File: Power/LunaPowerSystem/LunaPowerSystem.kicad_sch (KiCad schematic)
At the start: 16 parts, among them U1 Power Distribution Panel, U2 E-STOP, U3 Mini Power Distribution Panel, U4 Jetson Nano

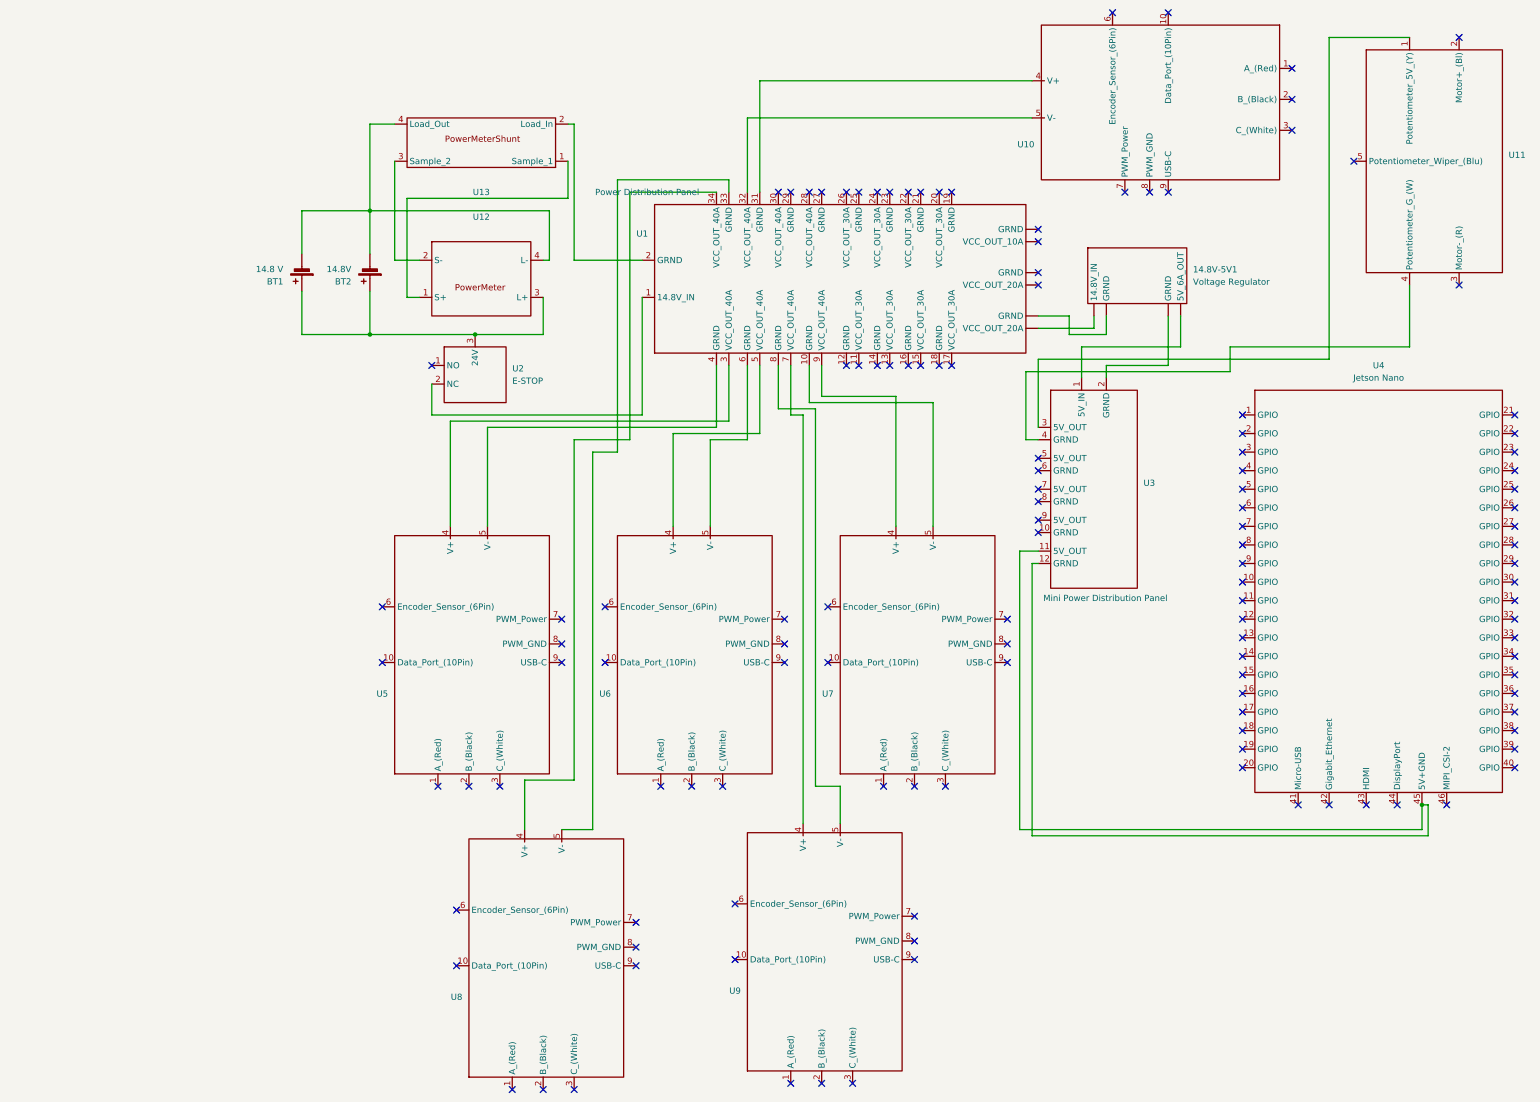
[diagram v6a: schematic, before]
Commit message: Refreshed changed symbols in Mech & Power Schematics
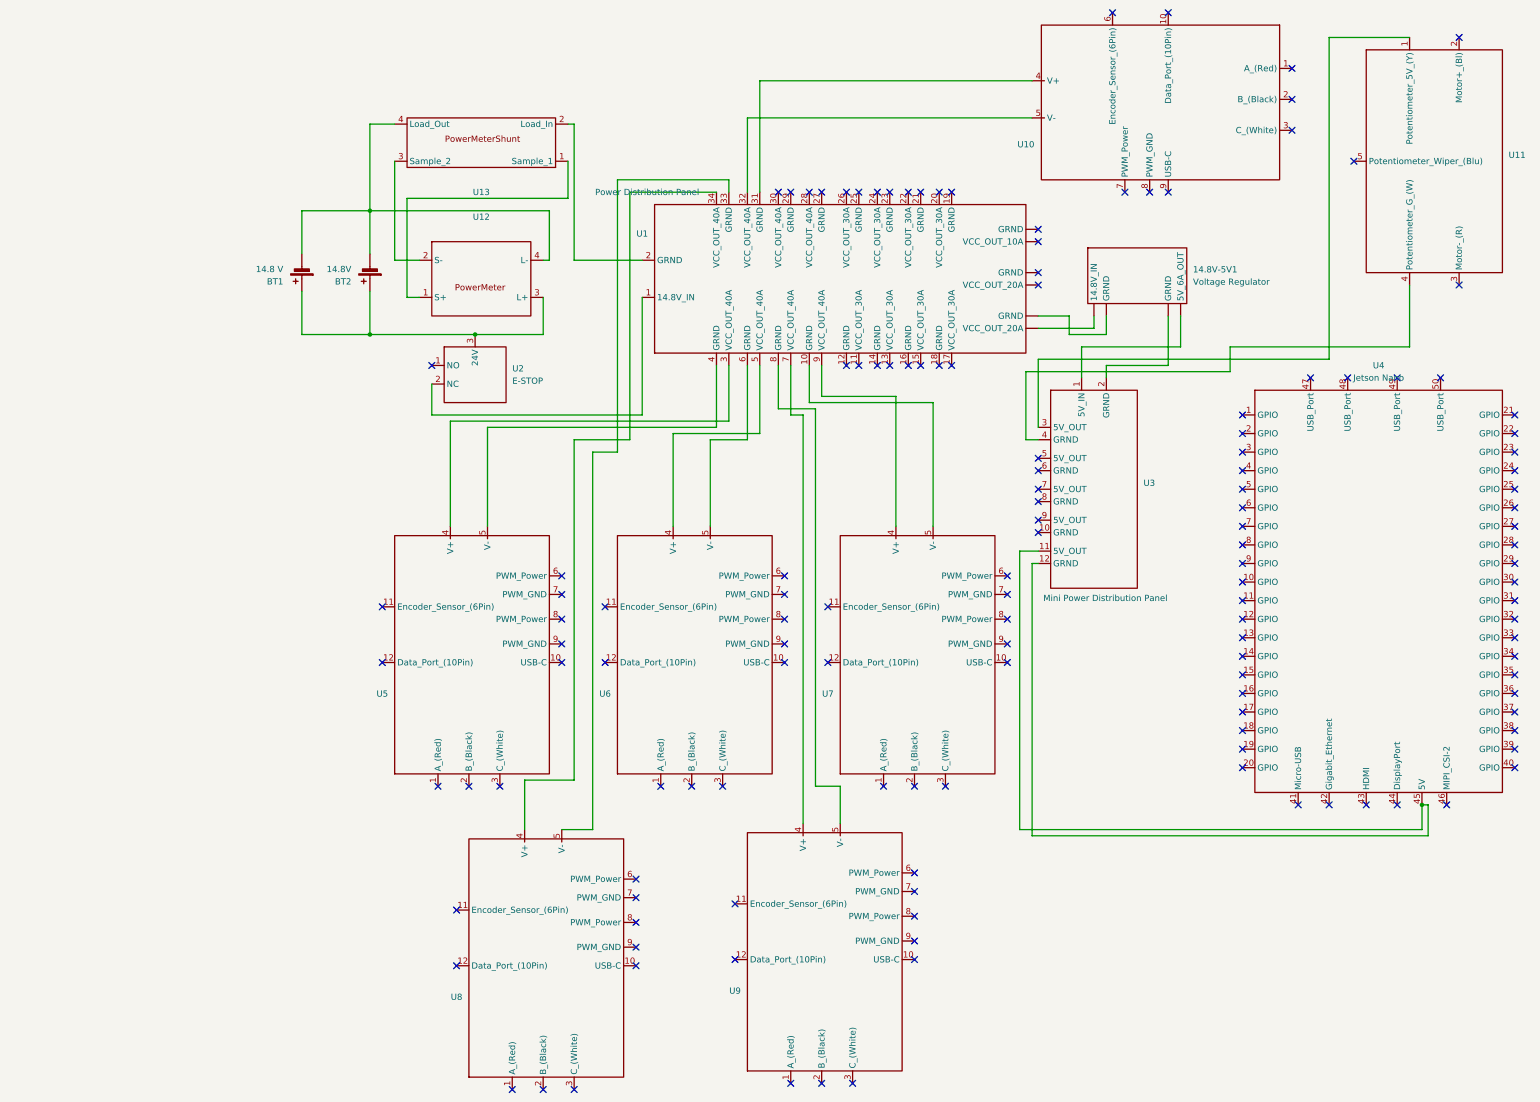
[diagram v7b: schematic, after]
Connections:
- net at U1. (GRND): now also 14.8V-5V1. (5V_6A_OUT)
- net at 14.8V-5V1. (5V_6A_OUT): now also U3.2 (GRND); no longer U1. (GRND)
- new net: 14.8V-5V1. (5V_6A_OUT), U1. (GRND)
- no-connect marks 127 -> 141
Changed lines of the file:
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@@
+	)
+	(no_connect
+		(at 227.33 130.81)
 	)
 	(no_connect
@@
 	)
 	(no_connect
+		(at 181.61 134.62)
+	)
+	(no_connect
 		(at 209.55 52.07)
 	)
@@
 	)
 	(no_connect
+		(at 181.61 130.81)
+	)
+	(no_connect
 		(at 138.43 236.22)
 	)
@@
 	)
 	(no_connect
+		(at 289.56 90.17)
+	)
+	(no_connect
 		(at 227.33 144.78)
 	)
@@
 	)
 	(no_connect
+		(at 227.33 134.62)
+	)
+	(no_connect
 		(at 275.59 151.13)
 	)
@@
 	)
 	(no_connect
+		(at 135.89 134.62)
+	)
+	(no_connect
 		(at 207.01 52.07)
 	)
 	(no_connect
+		(at 135.89 130.81)
+	)
+	(no_connect
 		(at 207.01 87.63)
 	)
@@
 	)
 	(no_connect
+		(at 151.13 196.85)
+	)
+	(no_connect
 		(at 227.33 148.59)
 	)
@@
 	)
 	(no_connect
+		(at 208.28 195.58)
+	)
+	(no_connect
 		(at 331.47 162.56)
 	)
@@
 	)
 	(no_connect
+		(at 316.23 90.17)
+	)
+	(no_connect
+		(at 208.28 191.77)
+	)
+	(no_connect
 		(at 331.47 113.03)
 	)
@@
 	)
 	(no_connect
+		(at 297.18 90.17)
+	)
+	(no_connect
 		(at 331.47 116.84)
 	)
@@
 	)
 	(no_connect
+		(at 307.34 90.17)
+	)
+	(no_connect
 		(at 194.31 52.07)
 	)
@@
 	(no_connect
 		(at 331.47 139.7)
+	)
+	(no_connect
+		(at 151.13 193.04)
 	)
 	(no_connect
@@
 	)
 	(symbol
+		(lib_name "Spark_MAX_Motor_Controller_4")
 		(lib_id "Lunabotics 2025-26:Spark_MAX_Motor_Controller")
 		(at 116.84 142.24 0)
@@
 		)
 		(pin "8"
+		)
+		(pin "12"
+		)
+		(pin "11"
 		)
 		(instances
@@
 		(pin "40"
 		)
+		(pin "50"
+		)
+		(pin "47"
+		)
+		(pin "48"
+		)
+		(pin "49"
+		)
 		(instances
 			(project ""
@@
 	)
 	(symbol
+		(lib_name "Spark_MAX_Motor_Controller_1")
 		(lib_id "Lunabotics 2025-26:Spark_MAX_Motor_Controller")
 		(at 208.28 142.24 0)
@@
 		(pin "8"
 		)
+		(pin "11"
+		)
+		(pin "12"
+		)
 		(instances
 			(project "LunaPowerSystem"
@@
 	)
 	(symbol
+		(lib_name "Spark_MAX_Motor_Controller_2")
 		(lib_id "Lunabotics 2025-26:Spark_MAX_Motor_Controller")
 		(at 189.23 203.2 0)
@@
 		(pin "8"
 		)
+		(pin "11"
+		)
+		(pin "12"
+		)
 		(instances
 			(project "LunaPowerSystem"
@@
 	)
 	(symbol
+		(lib_name "Spark_MAX_Motor_Controller_3")
 		(lib_id "Lunabotics 2025-26:Spark_MAX_Motor_Controller")
 		(at 162.56 142.24 0)
@@
 		)
 		(pin "8"
+		)
+		(pin "11"
+		)
+		(pin "12"
 		)
 		(instances
@@
 	)
 	(symbol
+		(lib_name "Spark_MAX_Motor_Controller_5")
 		(lib_id "Lunabotics 2025-26:Spark_MAX_Motor_Controller")
 		(at 132.08 204.47 0)
@@
 		(pin "8"
 		)
+		(pin "12"
+		)
+		(pin "11"
+		)
 		(instances
